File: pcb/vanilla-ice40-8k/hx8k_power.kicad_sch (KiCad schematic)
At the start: 36 parts, among them U1 ICE40HX8K-CT256

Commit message: [hx8k][pcb] move programmer to symbol lib
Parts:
- R10, R11: symbol !Misc:R_2.2K_0603 -> !Misc:R_100_0603; Digi-Key Part Number CR0603-FX-1000ELFCT-ND -> CR0603-FX-5102ELFCT-ND; LCSC Part # C22775 -> C23196
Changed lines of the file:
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@@
 	)
 	(symbol
-		(lib_id "!Misc:R_2.2K_0603")
+		(lib_id "!Misc:R_100_0603")
 		(at 158.75 38.1 0)
 		(unit 1)
@@
 			)
 		)
-		(property "Description" "Resistor, small symbol"
-			(at 158.75 38.1 0)
-			(effects
-				(font
-					(size 1.27 1.27)
-				)
-				(hide yes)
-			)
-		)
-		(property "LCSC Part #" "C22775"
-			(at 158.75 38.1 0)
-			(effects
-				(font
-					(size 1.27 1.27)
-				)
-				(hide yes)
-			)
-		)
-		(property "Digi-Key Part Number" "CR0603-FX-1000ELFCT-ND"
+		(property "Description" "51K 0603 Resistor"
+			(at 158.75 38.1 0)
+			(effects
+				(font
+					(size 1.27 1.27)
+				)
+				(hide yes)
+			)
+		)
+		(property "LCSC Part #" "C23196"
+			(at 158.75 38.1 0)
+			(effects
+				(font
+					(size 1.27 1.27)
+				)
+				(hide yes)
+			)
+		)
+		(property "Digi-Key Part Number" "CR0603-FX-5102ELFCT-ND"
 			(at 158.75 38.1 0)
 			(effects
@@
 	)
 	(symbol
-		(lib_id "!Misc:R_2.2K_0603")
+		(lib_id "!Misc:R_100_0603")
 		(at 181.61 38.1 0)
 		(unit 1)
@@
 			)
 		)
-		(property "Description" "Resistor, small symbol"
-			(at 181.61 38.1 0)
-			(effects
-				(font
-					(size 1.27 1.27)
-				)
-				(hide yes)
-			)
-		)
-		(property "LCSC Part #" "C22775"
-			(at 181.61 38.1 0)
-			(effects
-				(font
-					(size 1.27 1.27)
-				)
-				(hide yes)
-			)
-		)
-		(property "Digi-Key Part Number" "CR0603-FX-1000ELFCT-ND"
-			(at 181.61 38.1 0)
-			(effects
+		(property "Description" "51K 0603 Resistor"
+			(at 181.61 38.1 0)
+			(effects
+				(font
+					(size 1.27 1.27)
+				)
+				(hide yes)
+			)
+		)
+		(property "LCSC Part #" "C23196"
+			(at 181.61 38.1 0)
+			(effects
+				(font
+					(size 1.27 1.27)
+				)
+				(hide yes)
+			)
+		)
+		(property "Digi-Key Part Number" "CR0603-FX-5102ELFCT-ND"
+			(at 181.61 38.1 0)
+			(effects

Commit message: [hx8k][pcb] convert all components to custom lib
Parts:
- U1: footprint ICE40HX8K-CT256:BGA256C80P16X16_1400X1400X170 -> !Misc:BGA256C80P16X16_1400X1400X170; symbol ICE40HX8K-CT256:ICE40HX8K-CT256 -> !Misc:ICE40HX8K-CT256; Availability In Stock -> (none); Check_prices https://www.snapeda.com/parts/ICE40HX8K-CT256/Lattice+Semic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 -> (none); Description_1 iCE40™ HX Field Programmable Gate Array (FPGA) IC 206 13107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 -> (none); MANUFACTURER Lattice Semiconductor -> (none); MF Lattice Semiconductor -> (none); MP ICE40HX8K-CT256 -> (none); PART_REV 3.4 -> (none); Package CABGA-256 Lattice Semiconductor -> (none); Price None -> (none); STANDARD IPC-7351B -> (none); SnapEDA_Link https://www.snapeda.com/parts/ICE40HX8K-CT256/Lattice+Semic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 -> (none)

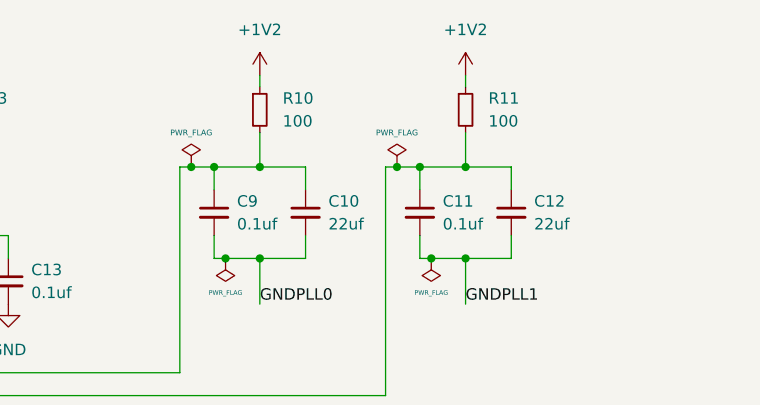
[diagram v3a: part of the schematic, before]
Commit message: [hx8k][pcb] fix 100ohm part numbers
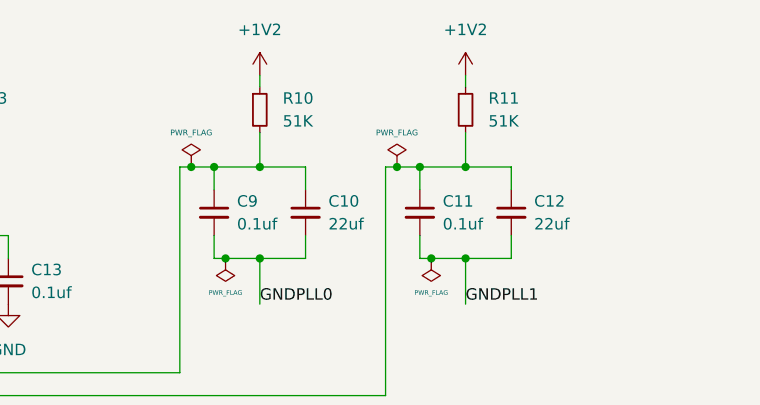
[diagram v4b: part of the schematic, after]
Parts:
- R10, R11: value 100 -> 51K; Digi-Key Part Number CR0603-FX-5102ELFCT-ND -> CR0603-FX-1000ELF
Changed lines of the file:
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@@
 			)
 		)
-		(property "Value" "100"
+		(property "Value" "51K"
 			(at 161.29 39.3699 0)
 			(effects
@@
 			)
 		)
-		(property "Description" "51K 0603 Resistor"
+		(property "Description" "100ohm 0603 Resistor"
 			(at 158.75 38.1 0)
 			(effects
@@
 			)
 		)
-		(property "Digi-Key Part Number" "CR0603-FX-5102ELFCT-ND"
+		(property "Digi-Key Part Number" "CR0603-FX-1000ELF"
 			(at 158.75 38.1 0)
 			(effects
@@
 			)
 		)
-		(property "Value" "100"
+		(property "Value" "51K"
 			(at 184.15 39.3699 0)
 			(effects
@@
 			)
 		)
-		(property "Description" "51K 0603 Resistor"
+		(property "Description" "100ohm 0603 Resistor"
 			(at 181.61 38.1 0)
 			(effects
@@
 			)
 		)
-		(property "Digi-Key Part Number" "CR0603-FX-5102ELFCT-ND"
+		(property "Digi-Key Part Number" "CR0603-FX-1000ELF"
 			(at 181.61 38.1 0)
 			(effects

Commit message: [hx8k][pcb] part cleanup
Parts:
- R10, R11: value 51K -> 100

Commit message: [hx8k][pcb] update part lib and reapply
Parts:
- R10, R11: LCSC Part # C23196 -> C22775
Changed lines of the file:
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@@
 			)
 		)
-		(property "LCSC Part #" "C23196"
+		(property "LCSC Part #" "C22775"
 			(at 158.75 38.1 0)
 			(effects
@@
 			)
 		)
-		(property "LCSC Part #" "C23196"
+		(property "LCSC Part #" "C22775"
 			(at 181.61 38.1 0)
 			(effects
